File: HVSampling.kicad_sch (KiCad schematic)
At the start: 52 parts, among them K5 SPU01M-05, U10 AMC1351, U5 AMC1351, U7 LM393, U8 4N35, U9 TLV6002

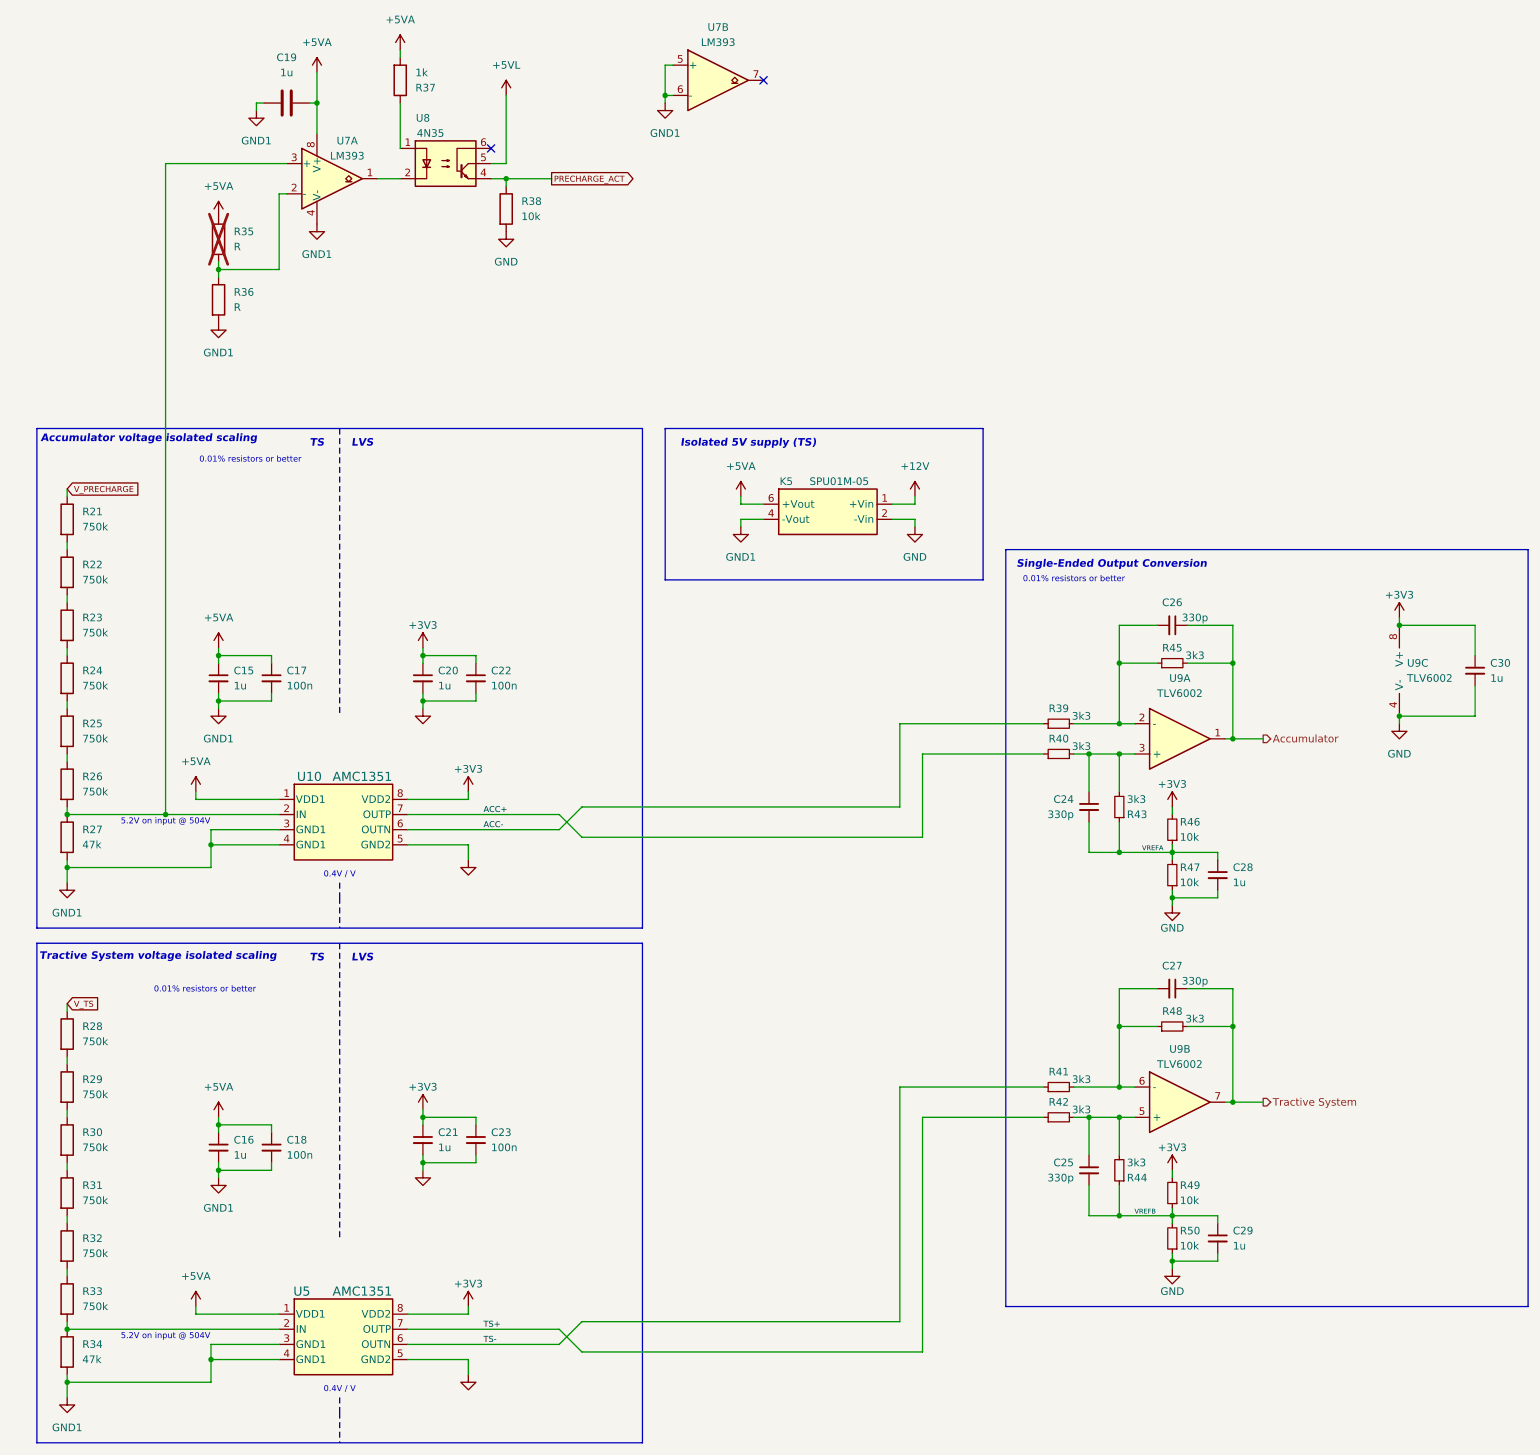
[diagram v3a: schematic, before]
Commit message: schematic: Create a hierarchical sheet for the isolated amplifiers
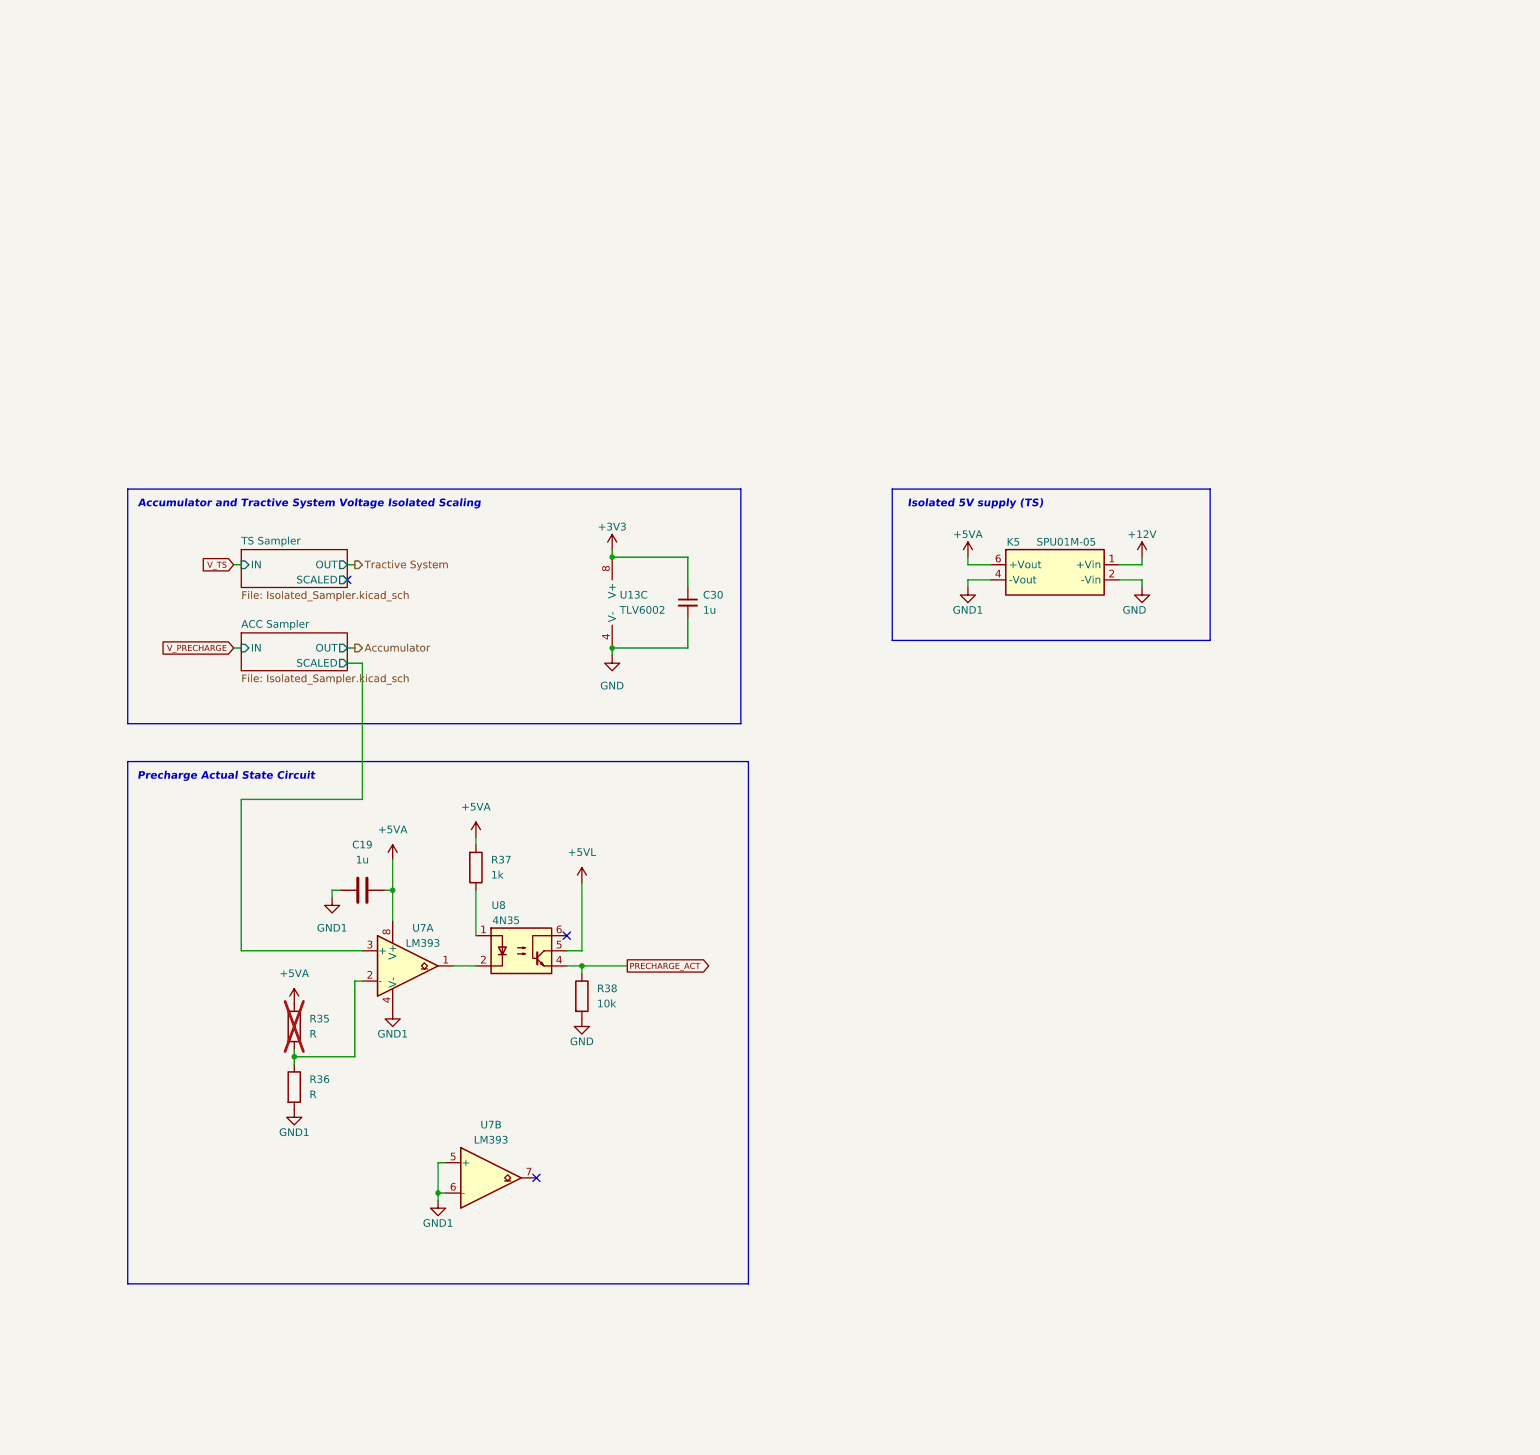
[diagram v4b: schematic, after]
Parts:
- removed C15, C16, C20, C21, C28, C29: 1u, Capacitor_SMD:C_0603_1608Metric, symbol Device:C_Small
- removed C17, C18, C22, C23: 100n, Capacitor_SMD:C_0603_1608Metric, symbol Device:C_Small
- removed C24, C25, C26, C27: 330p, Capacitor_SMD:C_0603_1608Metric, symbol Device:C_Small
- removed R21, R22, R23, R24, R25, R26, R28, R29, R30, R31, R32, R33: 750k, Resistor_SMD:R_0805_2012Metric, symbol Device:R
- removed R27, R34: 47k, Resistor_SMD:R_0805_2012Metric, symbol Device:R
- removed R39, R40, R41, R42, R43, R44, R45, R48: 3k3, Resistor_SMD:R_0603_1608Metric, symbol Device:R_Small
- removed R46, R47, R49, R50: 10k, Resistor_SMD:R_0603_1608Metric, symbol Device:R_Small
- removed U10, U5: AMC1351, Package_SO:SOIC-8_3.9x4.9mm_P1.27mm, symbol yfs:AMC1351
- removed unit 2 of U9
- removed unit 1 of U9
- renumbered U9 to U13
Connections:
- net ACC Sampler/SCALED: now reaches U7.3 (+)
- no-connect marks 2 -> 3
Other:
- added sheet ACC Sampler (Isolated_Sampler.kicad_sch)
- added sheet TS Sampler (Isolated_Sampler.kicad_sch)
- note added: "Accumulator and Tractive System Voltage Isolated Scaling"
- note added: "Precharge Actual State Circuit"
- note removed: "0.01% resistors or better"
- note removed: "0.4V / V"
- note removed: "5.2V on input @ 504V"
- note removed: "Accumulator voltage isolated scaling"
- note removed: "LVS"
- note removed: "Single-Ended Output Conversion"
- note removed: "TS"
- note removed: "Tractive System voltage isolated scaling"
- moved on the sheet: C19, C30, K5, R35, R36, R37, R38, U13C, U7A, U7B, U8

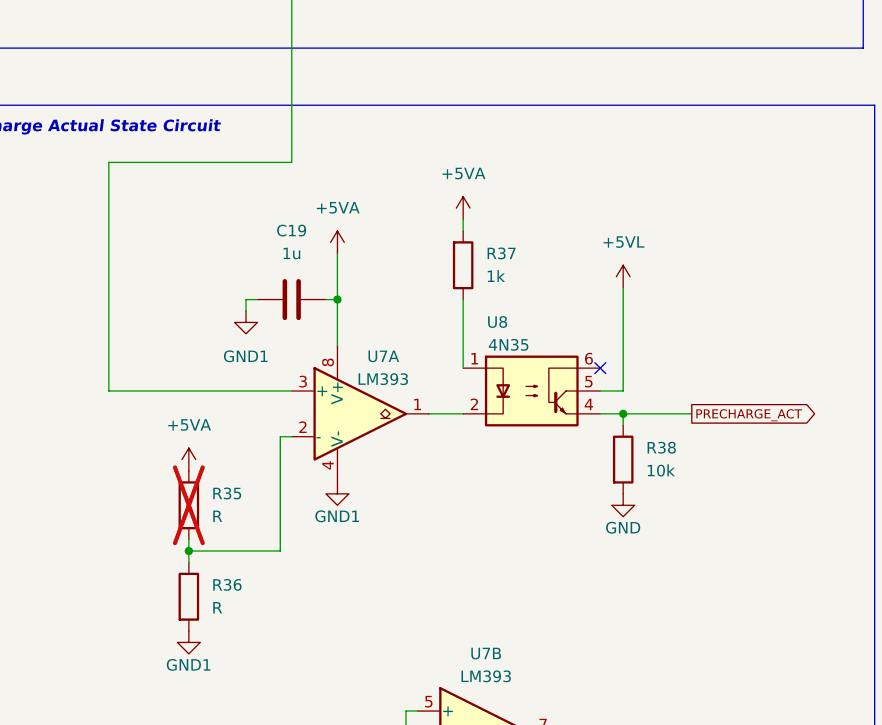
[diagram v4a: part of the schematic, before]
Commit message: schematic: Add a 200k pull-down to the 4N35 base
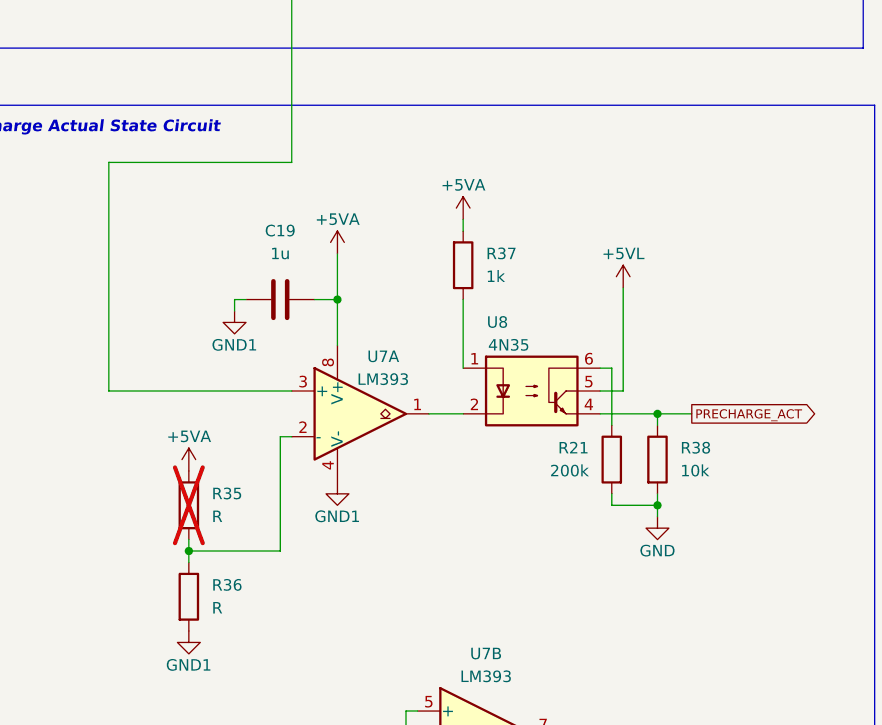
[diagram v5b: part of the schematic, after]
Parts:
- added R21: 200k, Resistor_SMD:R_0603_1608Metric, symbol Device:R
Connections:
- net GND: now also R21.2
- net at U8.6: now also R21.1
- no-connect marks 3 -> 2
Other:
- moved on the sheet: C19, R38
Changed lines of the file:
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@@
+	)
+	(junction
+		(at 110.49 115.57)
+		(diameter 0)
+		(color 0 0 0 0)
 	)
 	(junction
@@
 	)
 	(junction
-		(at 106.68 105.41)
+		(at 110.49 105.41)
 		(diameter 0)
 		(color 0 0 0 0)
@@
 	)
 	(no_connect
-		(at 104.14 100.33)
-	)
-	(no_connect
 		(at 99.06 140.97)
 	)
@@
 	(wire
 		(pts
-			(xy 64.77 93.98) (xy 64.77 92.71)
-		)
-		(stroke
-			(width 0)
-			(type default)
-		)
-	)
-	(wire
-		(pts
-			(xy 73.66 92.71) (xy 74.93 92.71)
+			(xy 63.5 93.98) (xy 63.5 92.71)
+		)
+		(stroke
+			(width 0)
+			(type default)
+		)
+	)
+	(wire
+		(pts
+			(xy 72.39 92.71) (xy 74.93 92.71)
 		)
 		(stroke
@@
 	(wire
 		(pts
+			(xy 110.49 115.57) (xy 110.49 114.3)
+		)
+		(stroke
+			(width 0)
+			(type default)
+		)
+	)
+	(wire
+		(pts
 			(xy 58.42 119.38) (xy 58.42 120.65)
 		)
@@
 	(wire
 		(pts
-			(xy 64.77 92.71) (xy 66.04 92.71)
+			(xy 63.5 92.71) (xy 64.77 92.71)
 		)
 		(stroke
@@
 	(wire
 		(pts
+			(xy 110.49 105.41) (xy 114.3 105.41)
+		)
+		(stroke
+			(width 0)
+			(type default)
+		)
+	)
+	(wire
+		(pts
 			(xy 171.45 41.91) (xy 171.45 40.64)
 		)
@@
 	(wire
 		(pts
+			(xy 110.49 116.84) (xy 110.49 115.57)
+		)
+		(stroke
+			(width 0)
+			(type default)
+		)
+	)
+	(wire
+		(pts
 			(xy 68.58 120.65) (xy 68.58 107.95)
 		)
@@
 	(wire
 		(pts
-			(xy 106.68 105.41) (xy 114.3 105.41)
-		)
-		(stroke
-			(width 0)
-			(type default)
-		)
-	)
-	(wire
-		(pts
 			(xy 124.46 46.99) (xy 124.46 52.07)
 		)
@@
 	(wire
 		(pts
-			(xy 106.68 105.41) (xy 106.68 106.68)
+			(xy 105.41 106.68) (xy 105.41 100.33)
+		)
+		(stroke
+			(width 0)
+			(type default)
+		)
+	)
+	(wire
+		(pts
+			(xy 110.49 105.41) (xy 110.49 106.68)
 		)
 		(stroke
@@
 	(wire
 		(pts
+			(xy 105.41 115.57) (xy 110.49 115.57)
+		)
+		(stroke
+			(width 0)
+			(type default)
+		)
+	)
+	(wire
+		(pts
 			(xy 124.46 36.83) (xy 111.76 36.83)
 		)
@@
 	(wire
 		(pts
+			(xy 105.41 100.33) (xy 104.14 100.33)
+		)
+		(stroke
+			(width 0)
+			(type default)
+		)
+	)
+	(wire
+		(pts
 			(xy 68.58 107.95) (xy 69.85 107.95)
 		)
@@
 	(wire
 		(pts
-			(xy 106.68 105.41) (xy 104.14 105.41)
+			(xy 105.41 114.3) (xy 105.41 115.57)
+		)
+		(stroke
+			(width 0)
+			(type default)
+		)
+	)
+	(wire
+		(pts
+			(xy 104.14 105.41) (xy 110.49 105.41)
 		)
 		(stroke
@@
 	(symbol
 		(lib_id "power:GND")
-		(at 106.68 114.3 0)
+		(at 110.49 116.84 0)
 		(unit 1)
 		(exclude_from_sim no)
@@
 		(dnp no)
 		(property "Reference" "#PWR082"
-			(at 106.68 120.65 0)
+			(at 110.49 123.19 0)
 			(effects
 				(font
@@
 		)
 		(property "Value" "GND"
-			(at 106.68 118.11 0)
+			(at 110.49 120.65 0)
 			(effects
 				(font
@@
 		)
 		(property "Footprint" ""
-			(at 106.68 114.3 0)
+			(at 110.49 116.84 0)
 			(effects
 				(font
@@
 		)
 		(property "Datasheet" ""
-			(at 106.68 114.3 0)
+			(at 110.49 116.84 0)
 			(effects
 				(font
@@
 		)
 		(property "Description" "Power symbol creates a global label with name \"GND\" , ground"
-			(at 106.68 114.3 0)
+			(at 110.49 116.84 0)
 			(effects
 				(font
@@
 		(on_board yes)
 		(dnp no)
-		(fields_autoplaced yes)
 		(property "Reference" "#PWR070"
 			(at 74.93 91.44 0)
@@
 		)
 		(property "Value" "+5VA"
-			(at 74.93 82.55 0)
+			(at 74.93 83.82 0)
 			(effects
 				(font
@@
 	)
 	(symbol
+		(lib_id "Device:R")
+		(at 105.41 110.49 0)
+		(mirror y)
+		(unit 1)
+		(exclude_from_sim no)
+		(in_bom yes)
+		(on_board yes)
+		(dnp no)
+		(property "Reference" "R21"
+			(at 102.87 109.22 0)
+			(effects
+				(font
+					(size 1.27 1.27)
+				)
+				(justify left)
+			)
+		)
+		(property "Value" "200k"
+			(at 102.87 111.76 0)
+			(effects
+				(font
+					(size 1.27 1.27)
+				)
+				(justify left)
+			)
+		)
+		(property "Footprint" "Resistor_SMD:R_0603_1608Metric"
+			(at 107.188 110.49 90)
+			(effects
+				(font
+					(size 1.27 1.27)
+				)
+				(hide yes)
+			)
+		)
+		(property "Datasheet" "~"
+			(at 105.41 110.49 0)
+			(effects
+				(font
+					(size 1.27 1.27)
+				)
+				(hide yes)
+			)
+		)
+		(property "Description" ""
+			(at 105.41 110.49 0)
+			(effects
+				(font
+					(size 1.27 1.27)
+				)
+				(hide yes)
+			)
+		)
+		(pin "1"
+		)
+		(pin "2"
+		)
+		(instances
+			(project "Precharge_PCB"
+				(path "/c467677d-b98c-4488-bd11-965ef67263b2/5111e28e-8231-41c0-b506-a567affaf28a"
+					(reference "R21")
+					(unit 1)
+				)
+			)
+		)
+	)
+	(symbol
 		(lib_id "power:+5VL")
 		(at 106.68 91.44 0)
@@
 		(on_board yes)
 		(dnp no)
-		(fields_autoplaced yes)
 		(property "Reference" "#PWR081"
 			(at 106.68 95.25 0)
@@
 		)
 		(property "Value" "+5VL"
-			(at 106.68 86.36 0)
+			(at 106.68 87.63 0)
 			(effects
 				(font
@@
 		(on_board yes)
 		(dnp no)
-		(fields_autoplaced yes)
 		(property "Reference" "#PWR063"
 			(at 58.42 115.57 0)
@@
 		)
 		(property "Value" "+5VA"
-			(at 58.42 106.68 0)
+			(at 58.42 107.95 0)
 			(effects
 				(font
@@
 	(symbol
 		(lib_id "Device:C")
-		(at 69.85 92.71 90)
+		(at 68.58 92.71 90)
 		(unit 1)
 		(exclude_from_sim no)
@@
 		(fields_autoplaced yes)
 		(property "Reference" "C19"
-			(at 69.85 85.09 90)
+			(at 68.58 85.09 90)
 			(effects
 				(font
@@
 		)
 		(property "Value" "1u"
-			(at 69.85 87.63 90)
+			(at 68.58 87.63 90)
 			(effects
 				(font
@@
 		)
 		(property "Footprint" "Capacitor_SMD:C_0603_1608Metric"
-			(at 73.66 91.7448 0)
+			(at 72.39 91.7448 0)
 			(effects
 				(font
@@
 		)
 		(property "Datasheet" "~"
-			(at 69.85 92.71 0)
+			(at 68.58 92.71 0)
 			(effects
 				(font
@@
 		)
 		(property "Description" ""
-			(at 69.85 92.71 0)
+			(at 68.58 92.71 0)
 			(effects
 				(font
@@
 	(symbol
 		(lib_id "power:GND1")
-		(at 64.77 93.98 0)
+		(at 63.5 93.98 0)
 		(unit 1)
 		(exclude_from_sim no)
@@
 		(on_board yes)
 		(dnp no)
-		(fields_autoplaced yes)
 		(property "Reference" "#PWR069"
-			(at 64.77 100.33 0)
+			(at 63.5 100.33 0)
 			(effects
 				(font
@@
 		)
 		(property "Value" "GND1"
-			(at 64.77 99.06 0)
+			(at 63.5 97.79 0)
 			(effects
 				(font
@@
 		)
 		(property "Footprint" ""
-			(at 64.77 93.98 0)
+			(at 63.5 93.98 0)
 			(effects
 				(font
@@
 		)
 		(property "Datasheet" ""
-			(at 64.77 93.98 0)
+			(at 63.5 93.98 0)
 			(effects
 				(font
@@
 		)
 		(property "Description" "Power symbol creates a global label with name \"GND1\" , ground"
-			(at 64.77 93.98 0)
+			(at 63.5 93.98 0)
 			(effects
 				(font
@@
 		(on_board yes)
 		(dnp no)
-		(fields_autoplaced yes)
 		(property "Reference" "#PWR072"
 			(at 88.9 87.63 0)
@@
 		)
 		(property "Value" "+5VA"
-			(at 88.9 78.74 0)
+			(at 88.9 80.01 0)
 			(effects
 				(font
@@
 	(symbol
 		(lib_id "Device:R")
-		(at 106.68 110.49 0)
+		(at 110.49 110.49 0)
 		(unit 1)
 		(exclude_from_sim no)
@@
 		(fields_autoplaced yes)
 		(property "Reference" "R38"
-			(at 109.22 109.22 0)
+			(at 113.03 109.22 0)
 			(effects
 				(font
@@
 		)
 		(property "Value" "10k"
-			(at 109.22 111.76 0)
+			(at 113.03 111.76 0)
 			(effects
 				(font
@@
 		)
 		(property "Footprint" "Resistor_SMD:R_0603_1608Metric"
-			(at 104.902 110.49 90)
+			(at 108.712 110.49 90)
 			(effects
 				(font
@@
 		)
 		(property "Datasheet" "~"
-			(at 106.68 110.49 0)
+			(at 110.49 110.49 0)
 			(effects
 				(font
@@
 		)
 		(property "Description" ""
-			(at 106.68 110.49 0)
-			(effects
-				(font
+			(at 110.49 110.49 0)
+			(effects
+				(font
